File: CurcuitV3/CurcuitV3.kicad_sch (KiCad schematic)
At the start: 92 parts, among them IC1 AS5600-ASOT, J1 Conn_01x07, J2 Conn_01x03, J3 Conn_01x02, J4 Conn_01x02, Q1 Q_NMOS_DGS, Q2 Q_NMOS_DGS, Q3 Q_NMOS_DGS, Q4 Q_NMOS_DGS, Q5 Q_NMOS_DGS, Q6 Q_NMOS_DGS, SW1 SW_Push, SW2 SW_Push, U1 DRV8300DPWR, U2 STM32F303K8Tx, U3 MCP9700x-ETT, U4 LM66100DCK, U7 AP7375-3.3, Y2 CSTNE16M0V530000R0

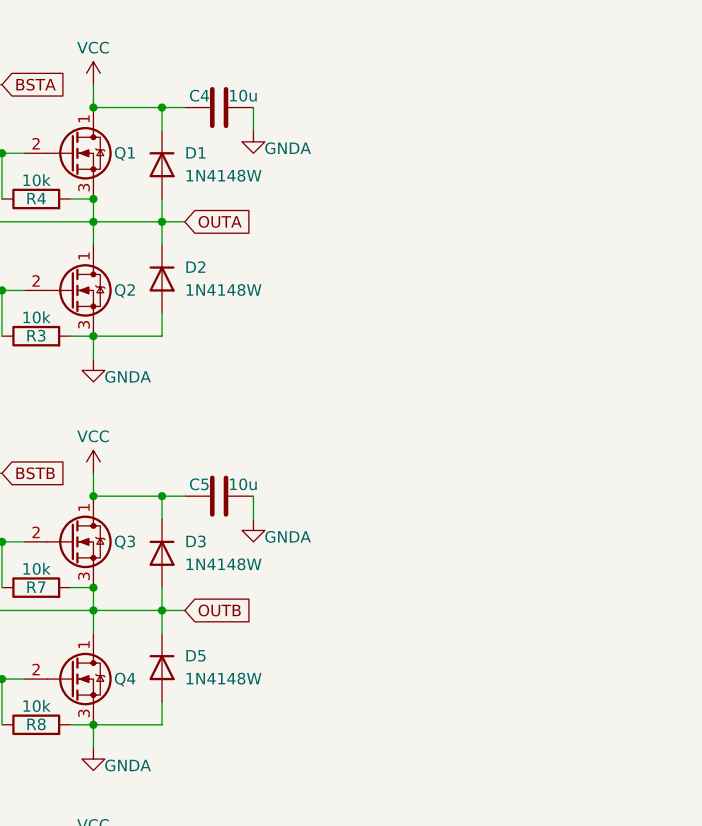
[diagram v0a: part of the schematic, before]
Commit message: 電流センス部品の追加
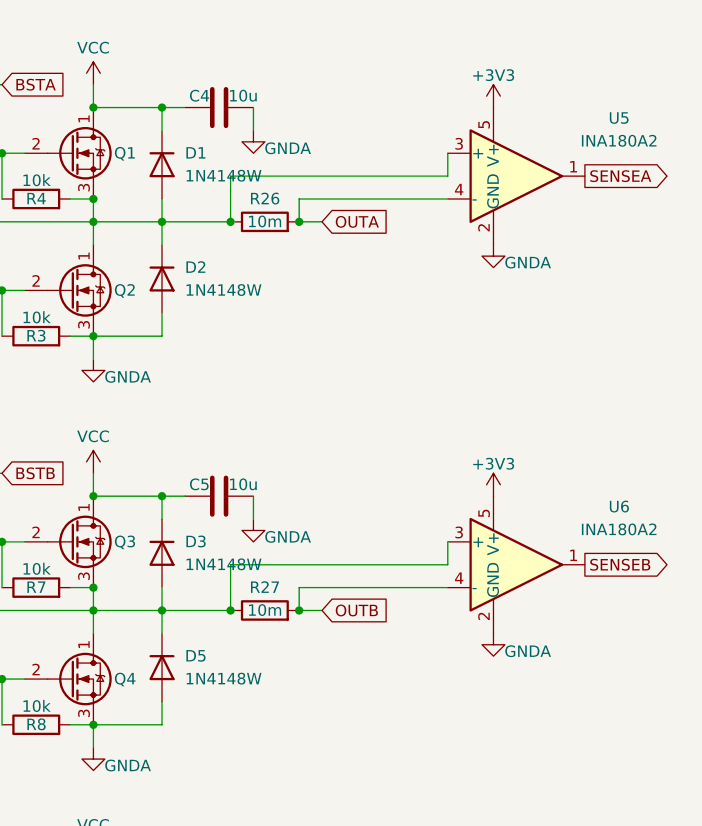
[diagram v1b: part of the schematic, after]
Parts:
- added R26, R27: 10m, Resistor_SMD:R_1206_3216Metric, symbol Device:R
- added U5, U6: INA180A2, Package_TO_SOT_SMD:SOT-23-5, symbol Amplifier_Current:INA180A2
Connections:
- net +3V3: now also U5.5 (V+), U6.5 (V+)
- net GNDA: now also U5.2 (GND), U6.2 (GND)
- net OUTA: now also R26.2, U5.4 (-); no longer C1.1, D1.2 (A), D2.1 (K), Q1.3 (S), Q2.1 (D), R4.2
- net OUTB: now also R27.2, U6.4 (-); no longer C2.1, D3.2 (A), D5.1 (K), Q3.3 (S), Q4.1 (D), R7.2
- new net: C2.1, D3.2 (A), D5.1 (K), Q3.3 (S), Q4.1 (D), R27.1, R7.2, U6.3 (+)
- new net: C1.1, D1.2 (A), D2.1 (K), Q1.3 (S), Q2.1 (D), R26.1, R4.2, U5.3 (+)
- new net SENSEA: U5.1
- new net SENSEB: U6.1

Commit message: 回路ほぼ完成
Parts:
- removed D1, D11, D12, D2, D3, D5: 1N4148W, Diode_SMD:D_SOD-123, symbol Diode:1N4148W
- removed H1, H2, H3, H4: MountingHole_Pad, MountingHole:MountingHole_3.2mm_M3_ISO14580_Pad_TopBottom, symbol Mechanical:MountingHole_Pad
- removed U5: INA180A2, Package_TO_SOT_SMD:SOT-23-5, symbol Amplifier_Current:INA180A2
- added C24: 0.1u, Capacitor_SMD:C_0603_1608Metric, symbol Device:C
- added D10, D3, D6, D7, D8, D9: D_Schottky, Diode_SMD:D_SOD-323_HandSoldering, symbol Device:D_Schottky
- added H1, H2, H3, H4: MountingHole, MountingHole:MountingHole_3.2mm_M3_ISO14580_Pad_TopBottom, symbol Mechanical:MountingHole
- added U6: INA180A2, Package_TO_SOT_SMD:SOT-23-5, symbol Amplifier_Current:INA180A2
- C10: renamed from C19; value 0.1u -> 10u
- C11: renamed from C18; value 0.1u -> 10u
- C12: renamed from C17; value 0.1u -> 10u
- C13: renamed from C16; value 0.1u -> 10u
- C14: renamed from C15; value 0.1u -> 10u
- C15: renamed from C14; value 0.1u -> 10u
- C20: renamed from C13; value 0.1u -> 10u
- C21: renamed from C12; value 0.1u -> 10u
- C4: renamed from C21; value 0.1u -> 10u
- C6: renamed from C20; value 0.1u -> 10u
- NT1: footprint NetTie:NetTie-2_SMD_Pad2.0mm -> NetTie:NetTie-2_SMD_Pad0.5mm
- renumbered C9 to C16, C10 to C17, C11 to C18, C26 to C19, C4 to C2, C3 to C22, C6 to C23, C8 to C25, C7 to C26, C24 to C3, C23 to C5, C22 to C7, C2 to C8, C5 to C9, D6 to D1, D4 to D11, D10 to D12, D7 to D2, D8 to D4, D9 to D5, J4 to J1, J1 to J3, J3 to J4, R15 to R1, R3 to R10, R20 to R11, R5 to R12, R7 to R13, R27 to R14, R6 to R15, R8 to R16, R23 to R17, R14 to R18, R9 to R19, R25 to R2, R11 to R20, R26 to R21, R10 to R22, R12 to R23, R21 to R24, R19 to R25, R24 to R26, R22 to R27, R16 to R3, R1 to R4, R17 to R5, R13 to R6, R4 to R7, R18 to R8, R2 to R9, TP5 to TP4, TP4 to TP5, U6 to U4, U4 to U5, Y2 to Y1
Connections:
- net +3V3: now also R11.1, U6.5 (V+); no longer R11.2
- net BUTTON: now also U2.21 (PA11); no longer U2.6 (PA0)
- net GND: now also U4.2 (GND), C24.1, U6.2 (GND)
- net GNDA: now also D10.2 (A), D6.2 (A), D8.2 (A); no longer U4.2 (GND)
- net OUTA: now also C1.1, Q1.3 (S), Q2.1 (D), R7.2, D3.2 (A), D6.1 (K); no longer R21.2
- net OUTC: now also R21.2, U6.4 (-); no longer C22.1, Q5.3 (S), Q6.1 (D), R20.2
- net SENSEB: now also U2.6 (PA0)
- net UART2_RX: now also R11.2; no longer R11.1
- net USB: now also U2.22 (PA12); no longer U2.7 (PA1)
- net VCC: now also D3.1 (K), D7.1 (K), D9.1 (K)
- net VOLTAGE: now also C24.2
- net at C8.1, Q3.3 (S), Q4.1 (D)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: now also D7.2 (A), D8.1 (K)
- net ENCODER_OUT renamed ENCODER
- new net: C22.1, D10.1 (K), D9.2 (A), Q5.3 (S), Q6.1 (D), R20.2, R21.1, U6.3 (+)
- new net SENSEC: U2.7 (PA1), U6.1
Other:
- note added: "STM32"
- moved on the sheet: C1, C10, C11, C12, C13, C14, C15, C16, C17, C18, C19, C2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

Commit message: ほぼ完成
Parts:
- removed C12, C20, C21, C4, C6: 10u, Capacitor_SMD:C_0805_2012Metric, symbol Device:C
- added C4, C7: 100u, Capacitor_THT:CP_Radial_D6.3mm_P2.50mm, symbol Device:C_Polarized
- C5: footprint Capacitor_SMD:C_0805_2012Metric -> Capacitor_SMD:C_0603_1608Metric
- J2: footprint Connector_JST:JST_XH_S3B-XH-A_1x03_P2.50mm_Horizontal -> Connector_Molex:Molex_SPOX_5268-03A_1x03_P2.50mm_Horizontal
- J4: footprint Connector_JST:JST_XH_S2B-XH-A_1x02_P2.50mm_Horizontal -> Connector_Molex:Molex_SPOX_5268-02A_1x02_P2.50mm_Horizontal
- U5: footprint Package_TO_SOT_SMD:SOT-363_SC-70-6 -> Package_TO_SOT_SMD:Texas_R-PDSO-G6
- renumbered C8 to C6, C7 to C8, R15 to R14, R16 to R15, R14 to R16, R22 to R21, R23 to R22, R24 to R23, R21 to R24
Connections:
- net BUTTON: now also U2.22 (PA12); no longer U2.21 (PA11)
- net OUTB: now also C6.1, D7.2 (A), D8.1 (K), Q3.3 (S), Q4.1 (D), R13.2; no longer R16.2, U4.4 (-)
- net OUTC: now also C22.1, D10.1 (K), D9.2 (A), Q5.3 (S), Q6.1 (D), R20.2; no longer R24.2, U6.4 (-)
- net USB: now also U2.21 (PA11); no longer U2.22 (PA12)
- net VCC: now also C4.1, C7.1
- net GNDA renamed GNDPWR
- net GNDPWR: now also R16.2, R24.2, U4.4 (-), U6.4 (-), C4.2, C7.2; no longer D10.2 (A), D8.2 (A), Q4.3 (S), Q6.3 (S), R15.2, R22.2
- new net: D10.2 (A), Q6.3 (S), R22.2, R24.1, U6.3 (+)
- new net: D8.2 (A), Q4.3 (S), R15.2, R16.1, U4.3 (+)
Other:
- note added: "BLDC"
- note added: "Supply"
- moved on the sheet: C13, C14, C15, C22, C23, C6, C9, D10, D7, D8, D9, H1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

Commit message: シルク書いた
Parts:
- added C12: 10u, Capacitor_SMD:C_0805_2012Metric, symbol Device:C
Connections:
- net +3V3: now also C12.1
- net GND: now also C12.2
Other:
- moved on the sheet: C25, C26, D11, U7

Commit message: V3の修正と製造ファイル生成
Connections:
- net GND: no longer U4.2 (GND), U6.2 (GND)
- net GNDPWR: now also U4.2 (GND), U6.2 (GND)
